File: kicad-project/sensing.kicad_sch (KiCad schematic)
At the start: 18 parts

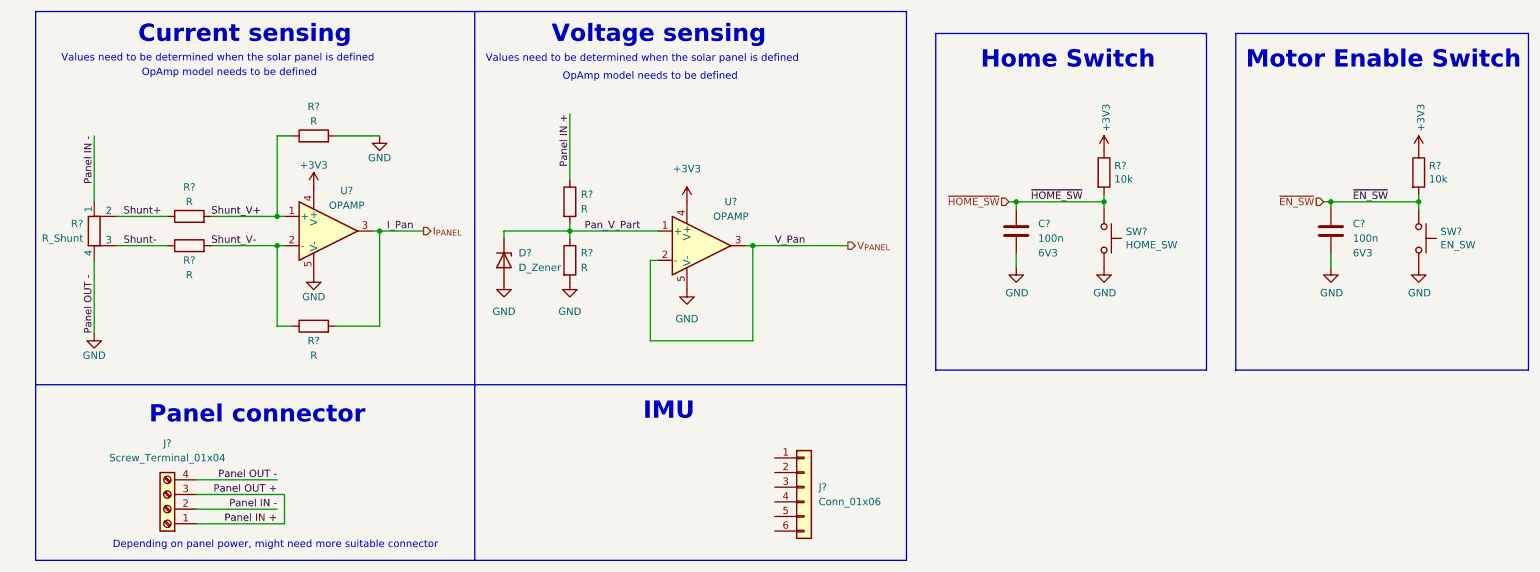
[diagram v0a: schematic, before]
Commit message: hw: add footprints for resistors and capacitors and re-add specs documant that was deleted
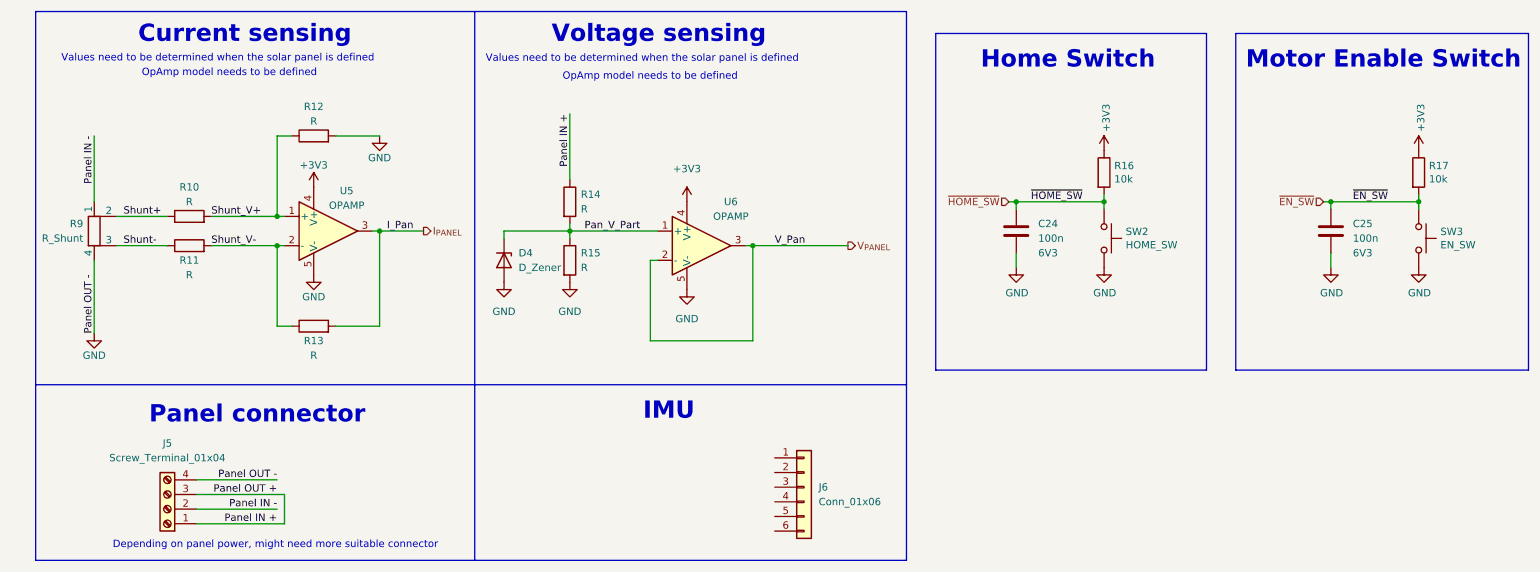
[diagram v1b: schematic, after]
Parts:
- C24, C25: renamed from C?; footprint (none) -> Capacitor_SMD:C_0603_1608Metric
- J5: renamed from J?; footprint (none) -> TerminalBlock_TE-Connectivity:TerminalBlock_TE_282834-4_1x04_P2.54mm_Horizontal
- J6: renamed from J?; footprint (none) -> Connector_PinHeader_2.54mm:PinHeader_1x06_P2.54mm_Vertical_SMD_Pin1Left
- R10, R11, R12, R13, R14, R15, R16, R17: renamed from R?; footprint (none) -> Resistor_SMD:R_0603_1608Metric
- gave numbers to parts that had none: 6

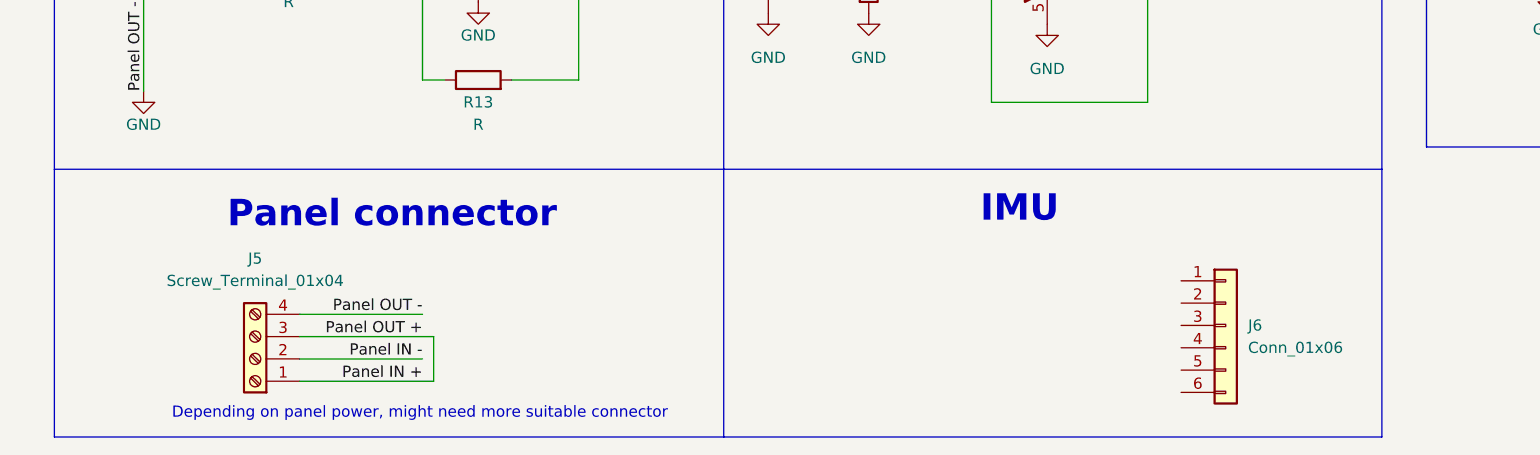
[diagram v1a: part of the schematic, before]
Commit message: hw: update root pin and usb connector
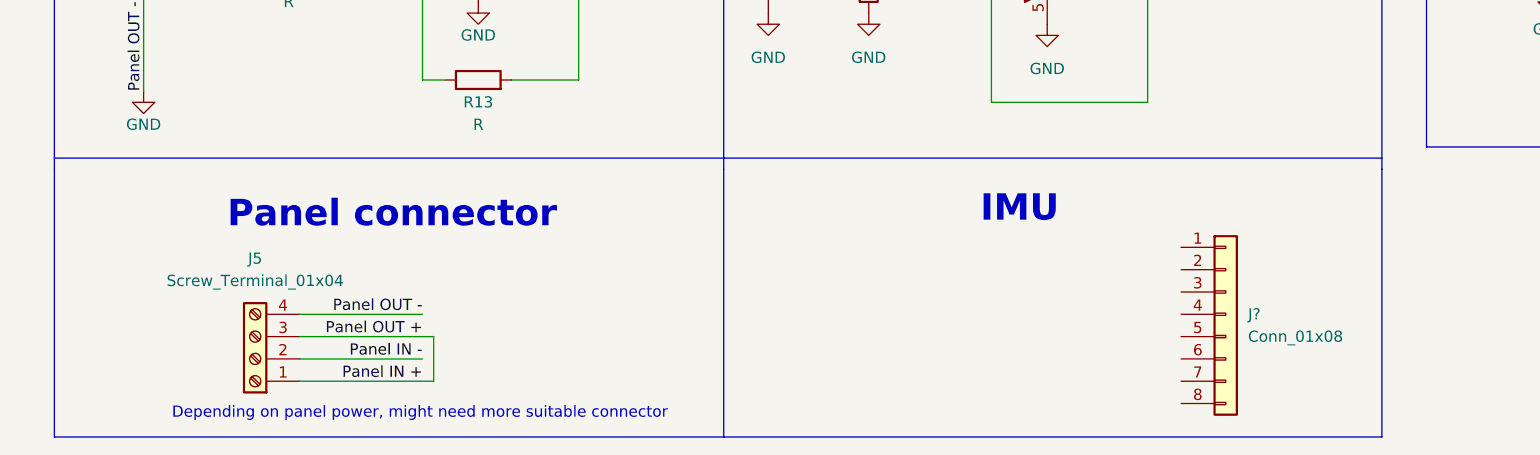
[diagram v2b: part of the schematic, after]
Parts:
- removed J6: Conn_01x06, Connector_PinHeader_2.54mm:PinHeader_1x06_P2.54mm_Vertical_SMD_Pin1Left, symbol Connector_Generic:Conn_01x06
- added J?: Conn_01x08, symbol Connector_Generic:Conn_01x08
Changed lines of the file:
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@@
     (stroke (width 0) (type default) (color 0 0 0 0))
   )
-  (polyline (pts (xy 165.1 78.74) (xy 90.17 78.74))
+  (polyline (pts (xy 165.1 77.47) (xy 90.17 77.47))
     (stroke (width 0) (type default) (color 0 0 0 0))
   )
@@
     (stroke (width 0) (type default) (color 0 0 0 0))
   )
-  (polyline (pts (xy 90.17 78.74) (xy 13.97 78.74))
+  (polyline (pts (xy 90.17 77.47) (xy 13.97 77.47))
     (stroke (width 0) (type default) (color 0 0 0 0))
   )
@@
     (pin "2")
   )
-  (symbol (lib_id "Connector_Generic:Conn_01x06") (at 147.32 96.52 0) (unit 1)
+  (symbol (lib_id "power:GND") (at 95.25 60.96 0) (unit 1)
+    (in_bom yes) (on_board yes)
+    (property "Reference" "#PWR055" (id 0) (at 95.25 67.31 0)
+      (effects (font (size 1.27 1.27)) hide)
+    )
+    (property "Value" "GND" (id 1) (at 95.25 66.04 0))
+    (property "Footprint" "" (id 2) (at 95.25 60.96 0)
+      (effects (font (size 1.27 1.27)) hide)
+    )
+    (property "Datasheet" "" (id 3) (at 95.25 60.96 0)
+      (effects (font (size 1.27 1.27)) hide)
+    )
+    (pin "1")
+  )
+  (symbol (lib_id "Device:R") (at 62.23 68.58 90) (unit 1)
+    (in_bom yes) (on_board yes)
+    (property "Reference" "R13" (id 0) (at 62.23 71.12 90))
+    (property "Value" "R" (id 1) (at 62.23 73.66 90))
+    (property "Footprint" "Resistor_SMD:R_0603_1608Metric" (id 2) (at 62.23 70.358 90)
+      (effects (font (size 1.27 1.27)) hide)
+    )
+    (property "Datasheet" "~" (id 3) (at 62.23 68.58 0)
+      (effects (font (size 1.27 1.27)) hide)
+    )
+    (pin "1")
+    (pin "2")
+  )
+  (symbol (lib_id "Connector_Generic:Conn_01x08") (at 147.32 95.25 0) (unit 1)
     (in_bom yes) (on_board yes) (fields_autoplaced)
-    (property "Reference" "J6" (id 0) (at 149.86 96.5199 0)
-      (effects (font (size 1.27 1.27)) (justify left))
-    )
-    (property "Value" "Conn_01x06" (id 1) (at 149.86 99.0599 0)
-      (effects (font (size 1.27 1.27)) (justify left))
-    )
-    (property "Footprint" "Connector_PinHeader_2.54mm:PinHeader_1x06_P2.54mm_Vertical_SMD_Pin1Left" (id 2) (at 147.32 96.52 0)
-      (effects (font (size 1.27 1.27)) hide)
-    )
-    (property "Datasheet" "~" (id 3) (at 147.32 96.52 0)
+    (property "Reference" "J?" (id 0) (at 149.86 95.2499 0)
+      (effects (font (size 1.27 1.27)) (justify left))
+    )
+    (property "Value" "Conn_01x08" (id 1) (at 149.86 97.7899 0)
+      (effects (font (size 1.27 1.27)) (justify left))
+    )
+    (property "Footprint" "" (id 2) (at 147.32 95.25 0)
+      (effects (font (size 1.27 1.27)) hide)
+    )
+    (property "Datasheet" "~" (id 3) (at 147.32 95.25 0)
       (effects (font (size 1.27 1.27)) hide)
     )
@@
     (pin "5")
     (pin "6")
-  )
-  (symbol (lib_id "power:GND") (at 95.25 60.96 0) (unit 1)
-    (in_bom yes) (on_board yes)
-    (property "Reference" "#PWR055" (id 0) (at 95.25 67.31 0)
-      (effects (font (size 1.27 1.27)) hide)
-    )
-    (property "Value" "GND" (id 1) (at 95.25 66.04 0))
-    (property "Footprint" "" (id 2) (at 95.25 60.96 0)
-      (effects (font (size 1.27 1.27)) hide)
-    )
-    (property "Datasheet" "" (id 3) (at 95.25 60.96 0)
-      (effects (font (size 1.27 1.27)) hide)
-    )
-    (pin "1")
-  )
-  (symbol (lib_id "Device:R") (at 62.23 68.58 90) (unit 1)
-    (in_bom yes) (on_board yes)
-    (property "Reference" "R13" (id 0) (at 62.23 71.12 90))
-    (property "Value" "R" (id 1) (at 62.23 73.66 90))
-    (property "Footprint" "Resistor_SMD:R_0603_1608Metric" (id 2) (at 62.23 70.358 90)
-      (effects (font (size 1.27 1.27)) hide)
-    )
-    (property "Datasheet" "~" (id 3) (at 62.23 68.58 0)
-      (effects (font (size 1.27 1.27)) hide)
-    )
-    (pin "1")
-    (pin "2")
+    (pin "7")
+    (pin "8")
   )
 )

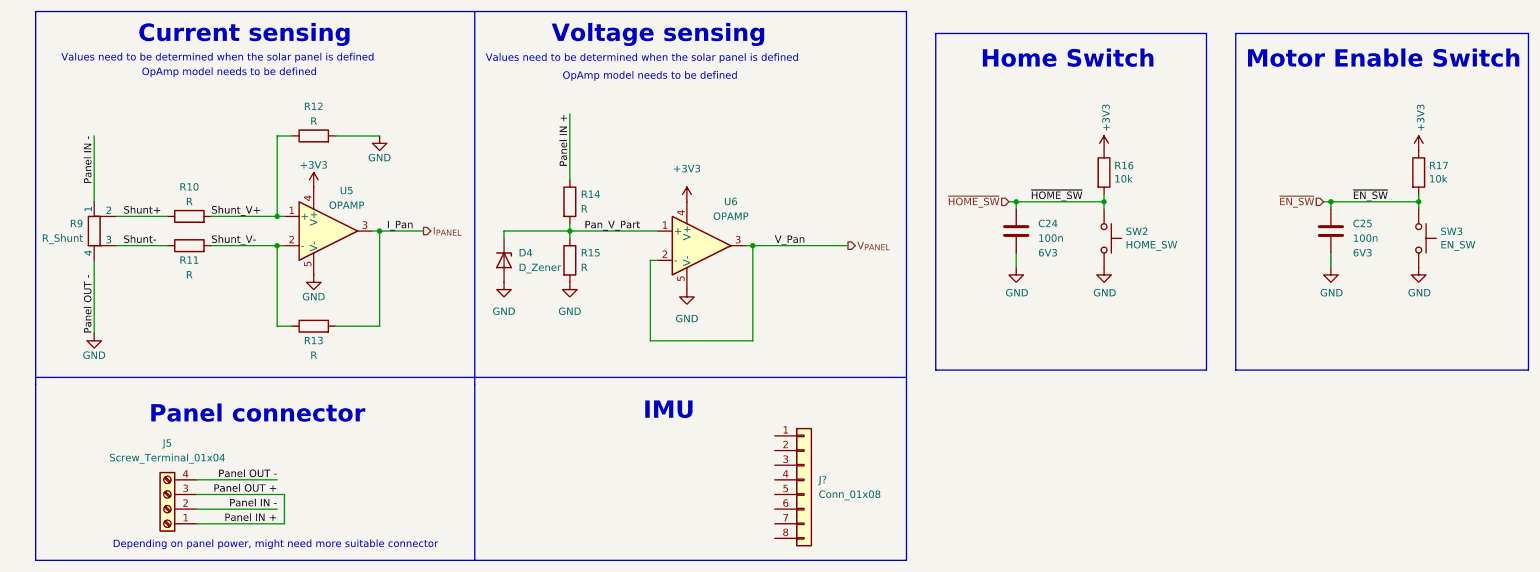
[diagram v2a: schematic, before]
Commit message: hw: part of last checks and footprint assignments
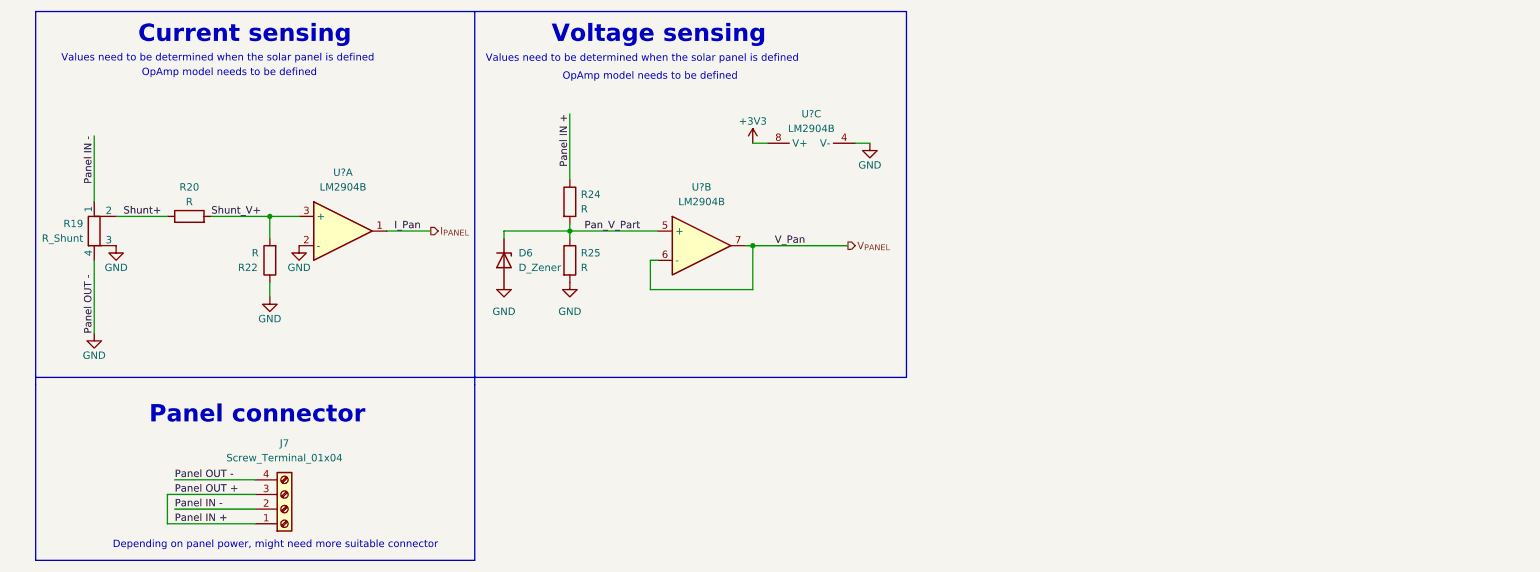
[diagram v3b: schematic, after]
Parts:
- removed C24, C25: 100n, Capacitor_SMD:C_0603_1608Metric, symbol Device:C
- removed J?: Conn_01x08, symbol Connector_Generic:Conn_01x08
- removed R11, R13: R, Resistor_SMD:R_0603_1608Metric, symbol Device:R
- removed R16, R17: 10k, Resistor_SMD:R_0603_1608Metric, symbol Device:R
- removed SW2: HOME_SW, symbol Switch:SW_Push
- removed SW3: EN_SW, symbol Switch:SW_Push
- removed U5, U6: OPAMP, symbol pspice:OPAMP
- added U? (x3): LM2904B, Package_SO:TSSOP-8_4.4x3mm_P0.65mm, symbol Device:Opamp_Dual
- D6: renamed from D4; footprint (none) -> Diode_SMD:D_0603_1608Metric
- R19: renamed from R9; footprint (none) -> Resistor_SMD:R_1210_3225Metric
- renumbered J5 to J7, R10 to R20, R12 to R22, R14 to R24, R15 to R25
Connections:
- net Shunt- is gone; now on net GND: R19.3
- net +3V3: now also U?.8 (V+)
- net GND: now also R22.1, U?.2 (-), U?.4 (V-); no longer R22.2
- net I_{PANEL}: now also U?.1
- net Pan_V_Part: now also U?.5 (+)
- net Shunt_V+: now also R22.2, U?.3 (+); no longer R22.1
- net V_{PANEL}: now also U?.6 (-), U?.7
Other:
- note removed: "Home Switch"
- note removed: "IMU"
- note removed: "Motor Enable Switch"
- moved on the sheet: J7, R22
